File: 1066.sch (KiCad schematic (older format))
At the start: 83 parts, among them J1 Conn_01x03, P1 Conn_01x50_Male_Atari_1066, P2 Conn_01x40_Male, SW1 Bank, U1 74LS156, U10 4164, U11 4164, U12 74LS157, U13 74LS257, U14 74LS257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

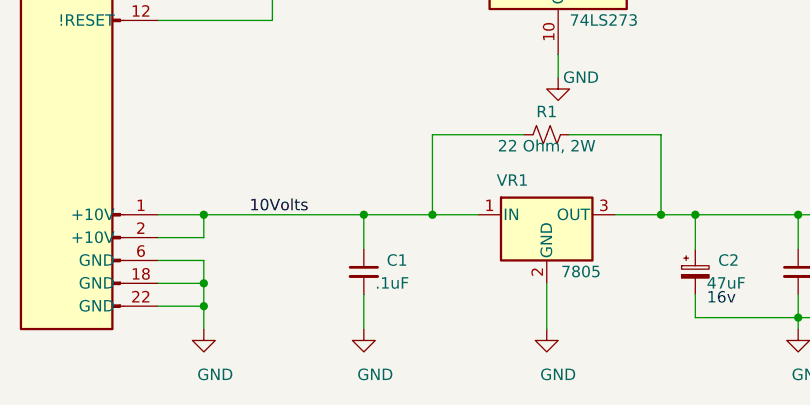
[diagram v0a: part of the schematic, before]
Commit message: apply fixes to sw1 c1 j1 and edge connector as pointed out by atari-passion on atariage.com
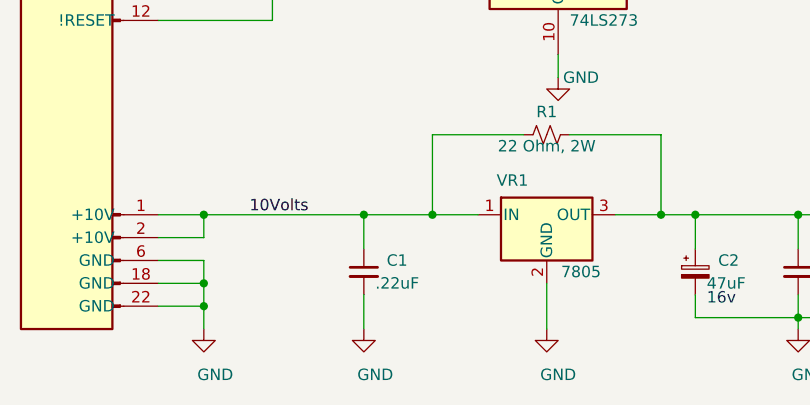
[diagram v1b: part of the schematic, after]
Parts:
- C1: value .1uF -> .22uF
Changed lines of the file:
@@
 P 2400 15300
 F 0 "C1" H 2500 15350 50  0000 L CNN
-F 1 ".1uF" H 2450 15250 50  0000 L CNN
+F 1 ".22uF" H 2450 15250 50  0000 L CNN
 F 2 "Capacitor_THT:C_Axial_L3.8mm_D2.6mm_P7.50mm_Horizontal" H 2400 15300 50  0001 C CNN
 F 3 "~" H 2400 15300 50  0001 C CNN

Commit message: fixed lower trace  by C11
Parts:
- U17: value 74LS51 -> 74S51
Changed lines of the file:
@@
 P 11450 7300
 F 0 "U17" H 10850 7950 50  0000 C CNN
-F 1 "74LS51" H 12000 6650 50  0000 C CNN
+F 1 "74S51" H 12000 6650 50  0000 C CNN
 F 2 "Package_DIP:DIP-14_W7.62mm_Socket" H 11450 7300 50  0001 L BNN
 F 3 "" H 11450 7300 50  0001 C CNN
@@
 P 15750 10100
 F 0 "U17" H 15900 10150 50  0000 L CNN
-F 1 "74LS51" H 15900 10050 50  0000 L CNN
+F 1 "74S51" H 15900 10050 50  0000 L CNN
 F 2 "Package_DIP:DIP-14_W7.62mm_Socket" H 15750 10100 50  0001 L BNN
 F 3 "" H 15750 10100 50  0001 C CNN
